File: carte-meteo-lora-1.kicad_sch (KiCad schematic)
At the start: 90 parts, among them J1 Conn_01x04, J2 USB_C_Receptacle_USB2.0_14P, J3 Conn_01x04, J4 Conn_01x04_Pin, J5 Conn_01x04, Q1 Q_NMOS, Q2 Q_NMOS, SW1 SW_SPST, U1 MS5607-02BA, U2 BQ77905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

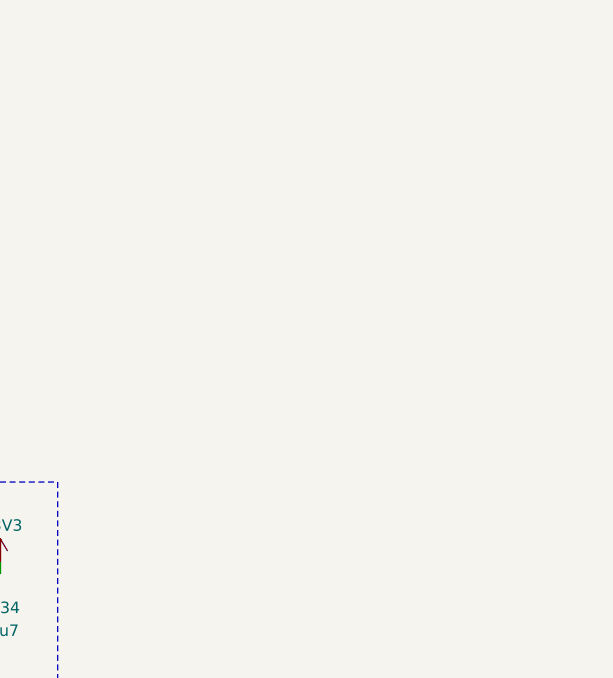
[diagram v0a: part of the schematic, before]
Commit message: schem: add SX1262 based lora module
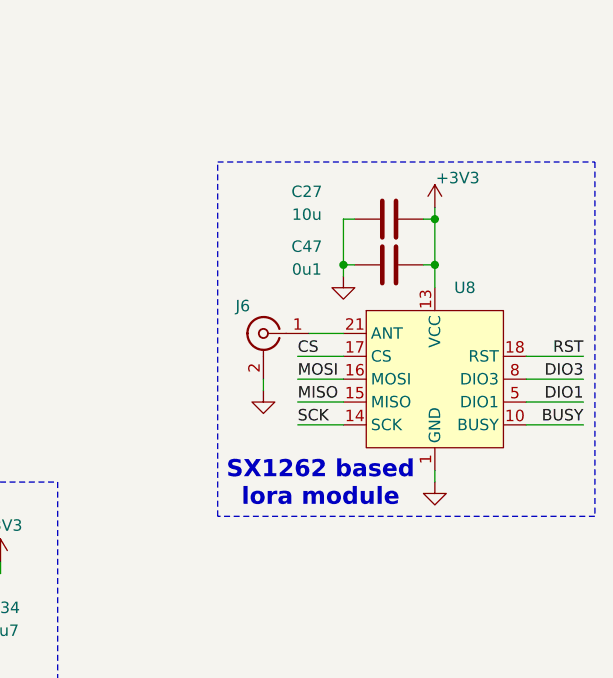
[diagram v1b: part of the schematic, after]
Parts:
- added C27: 10u, Capacitor_SMD:C_0402_1005Metric, symbol Device:C
- added C47: 0u1, Capacitor_SMD:C_0402_1005Metric, symbol Device:C
- added J6: Conn_Coaxial, symbol Connector:Conn_Coaxial
- added U8: (no value), symbol GLCS:SX1262TR8-GC
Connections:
- net +3V3: now also C27.1, C47.2, U8.13 (VCC)
- net GND: now also C27.2, C47.1, J6.2 (Ext), U8.1 (GND), U8.11 (GND), U8.12 (GND), U8.19 (GND), U8.2 (GND), U8.20 (GND), U8.22 (GND), U8.3 (GND), U8.4 (GND)
- new net: J6.1 (In), U8.21 (ANT)
- new net: U8.6 (NC), U8.7 (NC), U8.9 (NC)
- new net BUSY: U8.10 (BUSY)
- new net CS: U8.17 (CS)
- new net DIO1: U8.5 (DIO1)
- new net DIO3: U8.8 (DIO3)
- new net MISO: U8.15 (MISO)
- new net MOSI: U8.16 (MOSI)
- new net RST: U8.18 (RST)
- new net SCK: U8.14 (SCK)
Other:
- note added: "SX1262 based lora module"

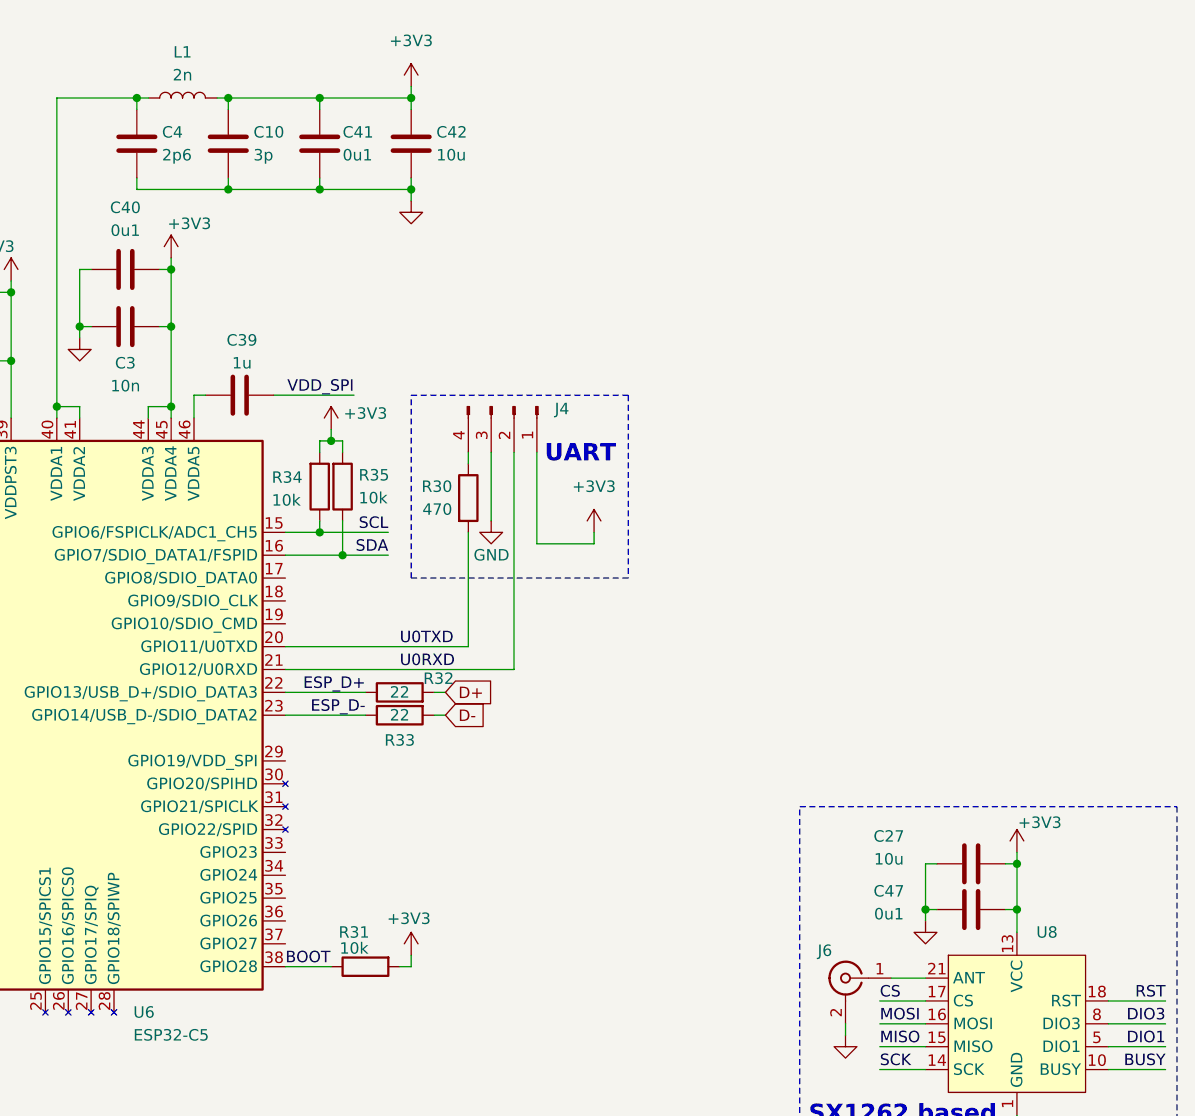
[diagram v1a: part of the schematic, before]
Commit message: schem: add ordering info to BOM
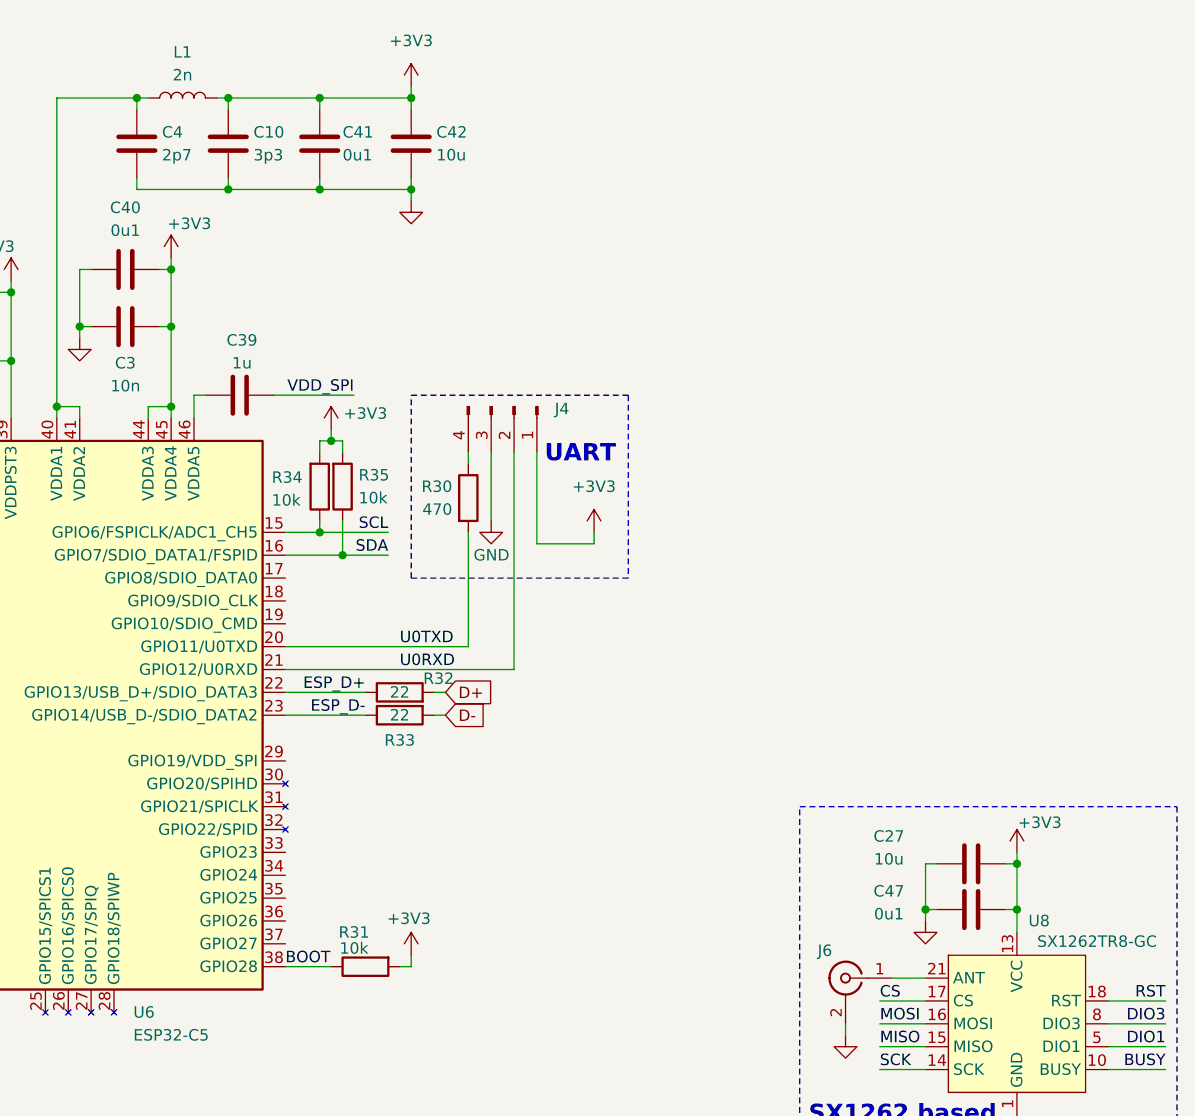
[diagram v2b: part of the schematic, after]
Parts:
- C1: footprint (none) -> Capacitor_SMD:C_0402_1005Metric; Basic (none) -> X; JLCPCB Part # (none) -> C327032; Manufacturer (none) -> YAGEO; Manufacturer Part Number (none) -> CC0402BRNPO9BNR80
- C10: value 3p -> 3p3; footprint (none) -> Capacitor_SMD:C_0402_1005Metric; Basic (none) -> Y; JLCPCB Part # (none) -> C1565; Manufacturer (none) -> FH (Guangdong Fenghua Advanced Tech); Manufacturer Part Number (none) -> 0402CG3R3C500NT
- C2: footprint (none) -> Capacitor_SMD:C_0402_1005Metric; Basic (none) -> X; JLCPCB Part # (none) -> C76909; Manufacturer (none) -> muRata; Manufacturer Part Number (none) -> GJM1555C1HR30WB01D
- C3: footprint (none) -> Capacitor_SMD:C_0402_1005Metric; Basic (none) -> Y; JLCPCB Part # (none) -> C15195; Manufacturer (none) -> Samsung Electro-Mechanics; Manufacturer Part Number (none) -> CL05B103KB5NNNC
- C4: value 2p6 -> 2p7; footprint (none) -> Capacitor_SMD:C_0402_1005Metric; Basic (none) -> Y; JLCPCB Part # (none) -> C15195; Manufacturer (none) -> Samsung Electro-Mechanics; Manufacturer Part Number (none) -> CL05B103KB5NNNC
- L1: footprint (none) -> Inductor_SMD:L_0402_1005Metric; Basic (none) -> X; JLCPCB Part # (none) -> C18216; Manufacturer (none) -> muRata; Manufacturer Part Number (none) -> LQG15HS2N0S02D
- U1: Basic (none) -> X; JLCPCB Part # (none) -> C97627; Manufacturer (none) -> TE Connectivity; Manufacturer Part Number (none) -> MS560702BA03-50
- U4: Basic (none) -> X; JLCPCB Part # (none) -> C2913569; Manufacturer (none) -> GXCAS; Manufacturer Part Number (none) -> GXHT30C
- U7: Basic (none) -> X; JLCPCB Part # (none) -> C83479; Manufacturer (none) -> TE Connectivity; Manufacturer Part Number (none) -> HTU21D
- U8: value (none) -> SX1262TR8-GC; Basic (none) -> X; JLCPCB Part # (none) -> C42381682; Manufacturer (none) -> Silicontra; Manufacturer Part Number (none) -> SX1262TR8-GC

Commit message: schem: fix BOM
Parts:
- C4: Basic Y -> E; JLCPCB Part # C15195 -> C1561; Manufacturer Samsung Electro-Mechanics -> FH (Guangdong Fenghua Advanced Tech); Manufacturer Part Number CL05B103KB5NNNC -> 0402CG2R7C500NT
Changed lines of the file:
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@@
 			)
 		)
-		(property "Basic" "Y"
+		(property "Basic" "E"
 			(at 227.33 27.94 0)
 			(hide yes)
@@
 			)
 		)
-		(property "JLCPCB Part #" "C15195"
+		(property "JLCPCB Part #" "C1561"
 			(at 227.33 27.94 0)
 			(hide yes)
@@
 			)
 		)
-		(property "Manufacturer" "Samsung Electro-Mechanics "
+		(property "Manufacturer" "FH (Guangdong Fenghua Advanced Tech)"
 			(at 227.33 27.94 0)
 			(hide yes)
@@
 			)
 		)
-		(property "Manufacturer Part Number" "CL05B103KB5NNNC"
+		(property "Manufacturer Part Number" "0402CG2R7C500NT"
 			(at 227.33 27.94 0)
 			(hide yes)

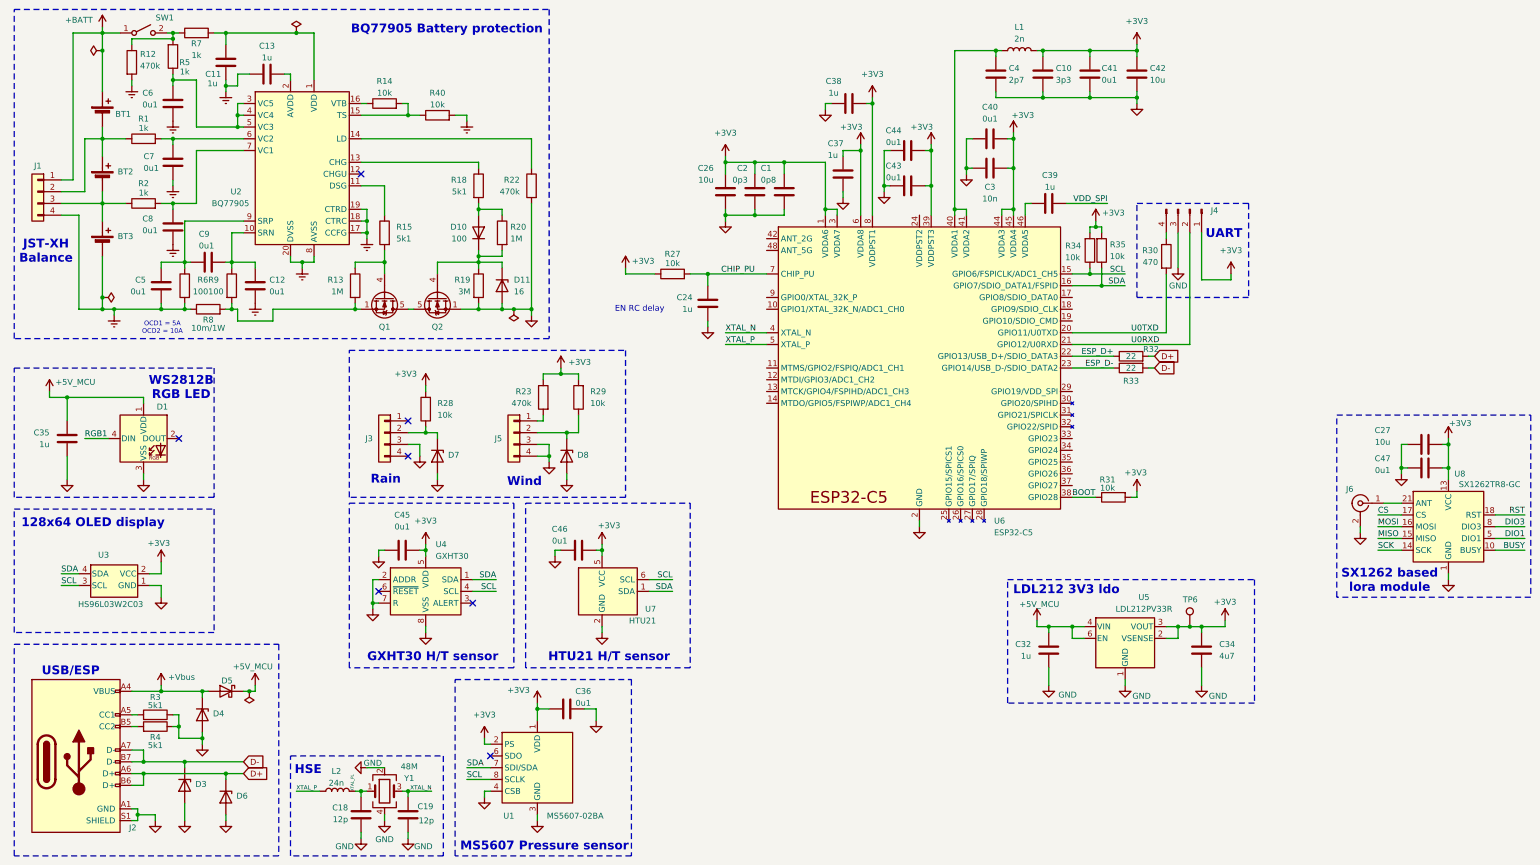
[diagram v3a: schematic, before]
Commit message: schem: add esp rf matching networks
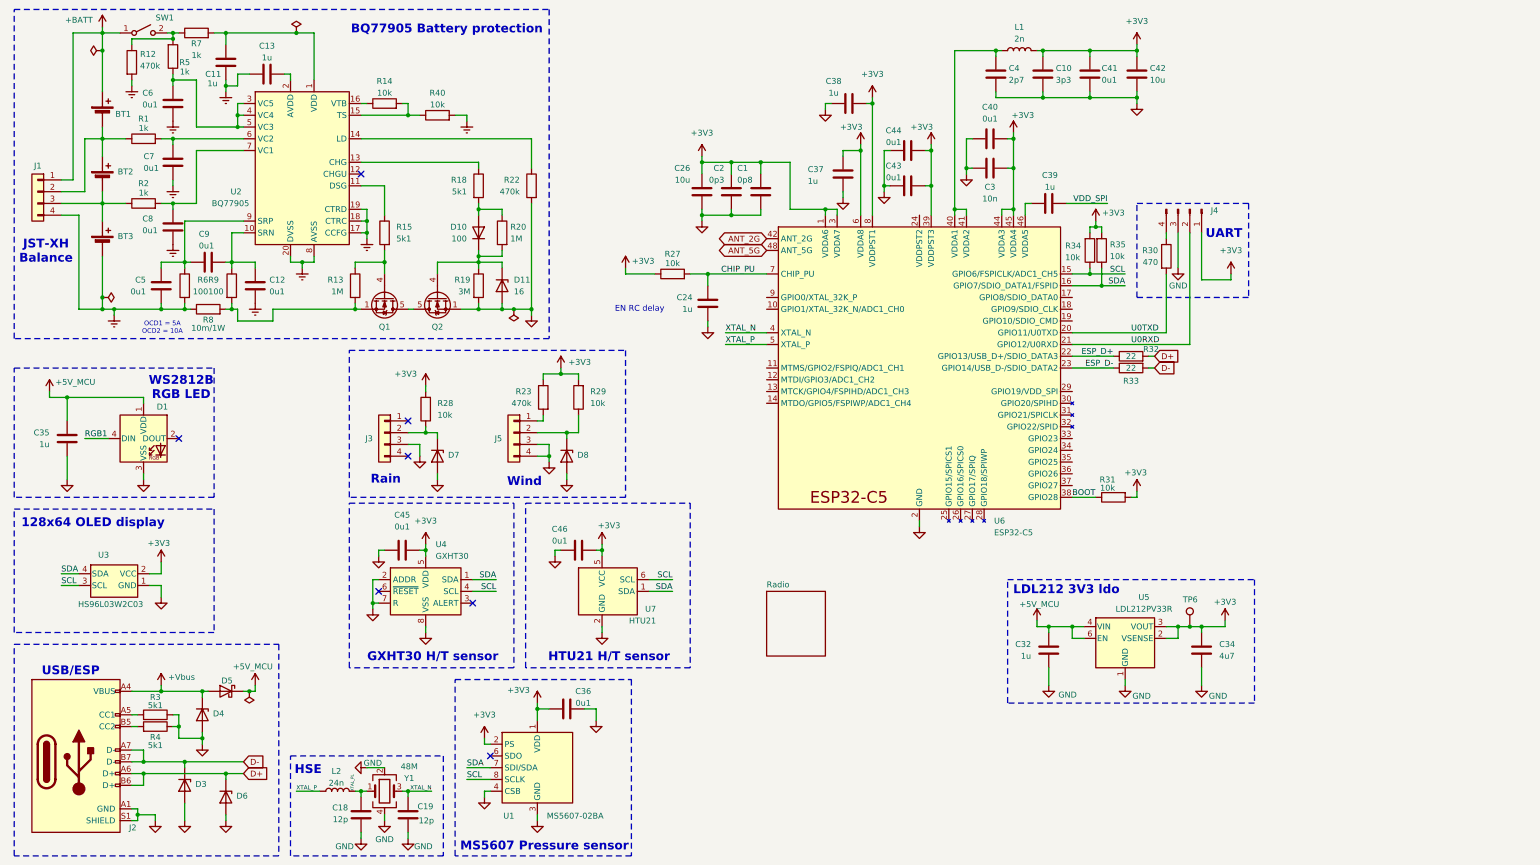
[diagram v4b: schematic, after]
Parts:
- removed C27: 10u, Capacitor_SMD:C_0402_1005Metric, symbol Device:C
- removed C47: 0u1, Capacitor_SMD:C_0402_1005Metric, symbol Device:C
- removed J6: Conn_Coaxial, symbol Connector:Conn_Coaxial
- removed U8: SX1262TR8-GC, symbol GLCS:SX1262TR8-GC
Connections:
- net ANT_2G: now reaches U6.42 (ANT_2G)
- net ANT_5G: now reaches U6.48 (ANT_5G)
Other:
- added sheet Radio (radio.kicad_sch)
- note removed: "SX1262 based lora module"
- moved on the sheet: C1, C2, C26

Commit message: schem: reorganize
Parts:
- removed BT1, BT2, BT3: Battery_Cell, symbol Device:Battery_Cell
- removed C11, C13, C32: 1u, Capacitor_SMD:C_0402_1005Metric, symbol Device:C
- removed C12, C5, C6, C7, C8, C9: 0u1, Capacitor_SMD:C_0402_1005Metric, symbol Device:C
- removed C34: 4u7, Capacitor_SMD:C_0402_1005Metric, symbol Device:C
- removed D10: 100, Diode_SMD:D_SOD-323, symbol Device:D
- removed D11: 16, Diode_SMD:D_SOD-123, symbol Device:D_Zener
- removed J1: Conn_01x04, Connector_JST:JST_XH_S4B-XH-A_1x04_P2.50mm_Horizontal, symbol Connector_Generic:Conn_01x04
- removed Q1, Q2: Q_NMOS, Package_SO:Vishay_PowerPAK_1212-8_Single, symbol Transistor_FET:SiS454DN
- removed R1, R2, R5, R7: 1k, Resistor_SMD:R_0402_1005Metric, symbol Device:R
- removed R12, R22: 470k, Resistor_SMD:R_0603_1608Metric, symbol Device:R
- removed R13, R20: 1M, Resistor_SMD:R_0402_1005Metric, symbol Device:R
- removed R14, R40: 10k, Resistor_SMD:R_0402_1005Metric, symbol Device:R
- removed R15, R18: 5k1, Resistor_SMD:R_0402_1005Metric, symbol Device:R
- removed R19: 3M, Resistor_SMD:R_0603_1608Metric, symbol Device:R
- removed R6, R9: 100, Resistor_SMD:R_0402_1005Metric, symbol Device:R
- removed R8: 10m/1W, Resistor_SMD:R_1206_3216Metric, symbol Device:R
- removed SW1: SW_SPST, Connector_PinHeader_2.54mm:PinHeader_1x02_P2.54mm_Vertical, symbol Switch:SW_SPST
- removed TP6: TestPoint, TestPoint:TestPoint_Pad_D2.0mm, symbol Connector:TestPoint
- removed U2: BQ77905, Package_SO:TSSOP-20_4.4x6.5mm_P0.65mm, symbol GLCS:BQ77905
- removed U5: LDL212PV33R, GLCS:DFN-6-1EP_2x2mm_P0.5mm_ST, symbol GLCS:LDL212PV33R
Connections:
- no-connect marks 7 -> 6
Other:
- added sheet Power (power.kicad_sch)
- note added: "MS5607 Pressure"
- note removed: "BQ77905 Battery protection"
- note removed: "JST-XH Balance"
- note removed: "LDL212 3V3 ldo"
- note removed: "MS5607 Pressure sensor"
- note removed: "OCD1 = 5A OCD2 = 10A"
- moved on the sheet: C1, C10, C18, C19, C2, C24, C26, C3, C35, C36, C37, C38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

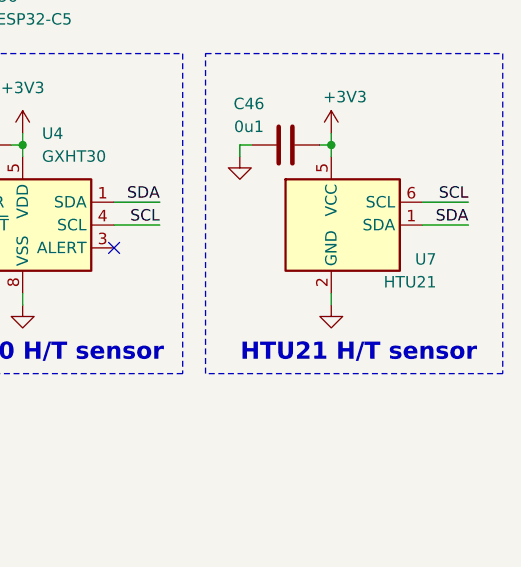
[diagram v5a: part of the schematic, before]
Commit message: schem: rf fix switchable connectors orientation
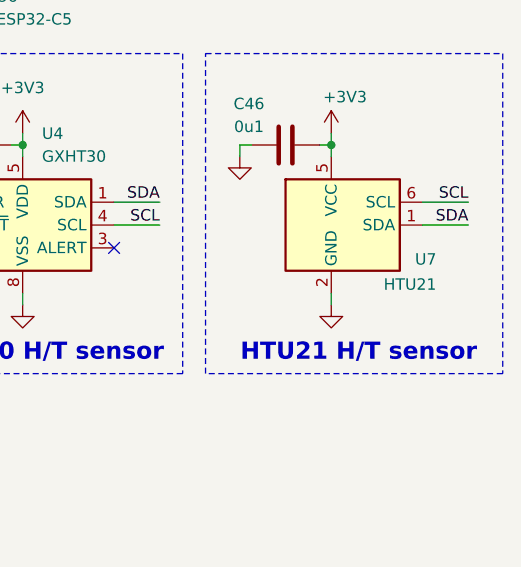
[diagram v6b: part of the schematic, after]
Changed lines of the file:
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@@
 		)
 		(property "Value" "HTU21"
-			(at 275.844 153.67 0)
+			(at 275.844 153.924 0)
 			(show_name no)
 			(do_not_autoplace no)

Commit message: schem: fix VDD_SPI cap
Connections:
- net GND: now also C39.2
- net VDD_SPI: now also C39.1, U6.46 (VDDA5); no longer C39.2
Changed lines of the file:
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@@
 	(wire
 		(pts
+			(xy 242.57 53.34) (xy 243.84 53.34)
+		)
+		(stroke
+			(width 0)
+			(type default)
+		)
+	)
+	(wire
+		(pts
 			(xy 41.91 189.23) (xy 40.64 189.23)
 		)
@@
 	(wire
 		(pts
-			(xy 242.57 53.34) (xy 251.46 53.34)
-		)
-		(stroke
-			(width 0)
-			(type default)
-		)
-	)
-	(wire
-		(pts
 			(xy 231.14 54.61) (xy 231.14 55.88)
 		)
@@
 	(wire
 		(pts
+			(xy 243.84 54.61) (xy 243.84 53.34)
+		)
+		(stroke
+			(width 0)
+			(type default)
+		)
+	)
+	(wire
+		(pts
 			(xy 60.96 179.07) (xy 64.77 179.07)
 		)
@@
 		)
 	)
-	(label "VDD_SPI"
-		(at 251.46 53.34 180)
+	(label "SDA"
+		(at 245.11 144.78 180)
 		(effects
 			(font
@@
 		)
 	)
-	(label "SDA"
-		(at 245.11 144.78 180)
+	(label "VDD_SPI"
+		(at 234.95 53.34 90)
 		(effects
 			(font
 				(size 1.27 1.27)
 			)
-			(justify right bottom)
+			(justify left bottom)
 		)
 	)
@@
 					(unit 1)
 				)
+			)
+		)
+	)
+	(symbol
+		(lib_id "power:GND")
+		(at 243.84 54.61 0)
+		(unit 1)
+		(body_style 1)
+		(exclude_from_sim no)
+		(in_bom yes)
+		(on_board yes)
+		(in_pos_files yes)
+		(dnp no)
+		(fields_autoplaced yes)
+		(property "Reference" "#PWR094"
+			(at 243.84 60.96 0)
+			(hide yes)
+			(show_name no)
+			(do_not_autoplace no)
+			(effects
+				(font
+					(size 1.27 1.27)
+				)
+			)
+		)
+		(property "Value" "GND"
+			(at 243.84 59.69 0)
+			(hide yes)
+			(show_name no)
+			(do_not_autoplace no)
+			(effects
+				(font
+					(size 1.27 1.27)
+				)
+			)
+		)
+		(property "Footprint" ""
+			(at 243.84 54.61 0)
+			(hide yes)
+			(show_name no)
+			(do_not_autoplace no)
+			(effects
+				(font
+					(size 1.27 1.27)
+				)
+			)
+		)
+		(property "Datasheet" ""
+			(at 243.84 54.61 0)
+			(hide yes)
+			(show_name no)
+			(do_not_autoplace no)
+			(effects
+				(font
+					(size 1.27 1.27)
+				)
+			)
+		)
+		(property "Description" "Power symbol creates a global label with name \"GND\" , ground"
+			(at 243.84 54.61 0)
+			(hide yes)
+			(show_name no)
+			(do_not_autoplace no)
+			(effects
+				(font
+					(size 1.27 1.27)
+				)
+			)
+		)
+		(pin "1"
+		)
+		(instances
+			(project "carte-meteo-lora-1"
+				(path "/13f499c2-4dc3-4e2c-8cf4-c7d5e00eb573"
+					(reference "#PWR094")
+					(unit 1)
+				)
